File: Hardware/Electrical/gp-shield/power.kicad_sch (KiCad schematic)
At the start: 32 parts, among them J1 XT60/TERM2, J2 XT60/TERM2, Q1 Q_PMOS_GDS, SW1 SW_SPDT, U1 NCP1117-5.0_SOT223, U2 LM4040DBZ-2.5, U4 LM397

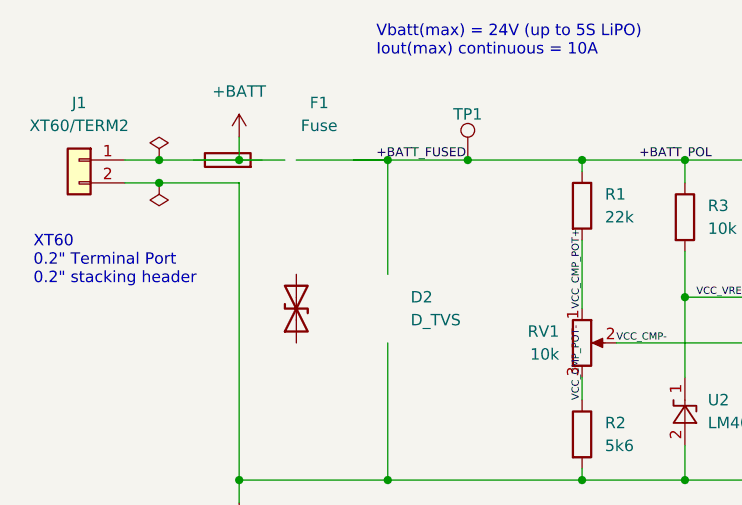
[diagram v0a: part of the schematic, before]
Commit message: Minor annotation fixes from merge
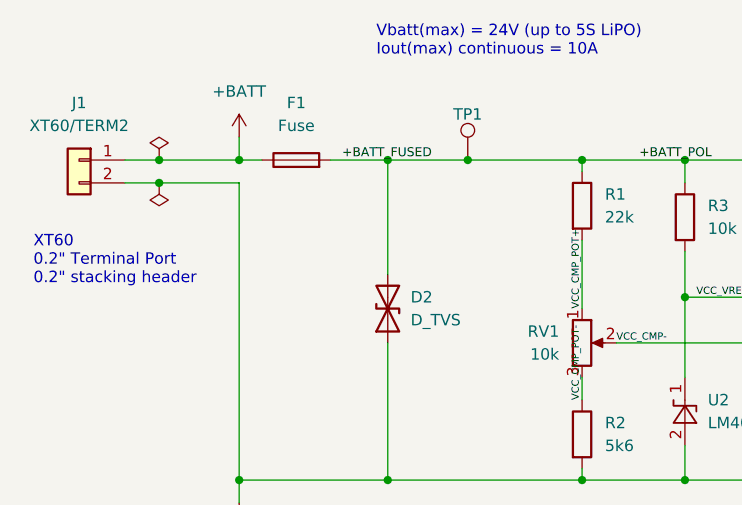
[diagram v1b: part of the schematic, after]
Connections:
- net +BATT: now also F1.1
- net +BATT_FUSED: now also D2.2 (A2), F1.2
- net GND: now also D2.1 (A1)
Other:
- moved on the sheet: D2, F1
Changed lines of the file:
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@@
-    (stroke (width 0) (type default) (color 0 0 0 0))
-  )
-  (wire (pts (xy 58.42 31.75) (xy 62.23 31.75))
     (stroke (width 0) (type default) (color 0 0 0 0))
   )
@@
     (stroke (width 0) (type default) (color 0 0 0 0))
   )
-  (wire (pts (xy 45.72 31.75) (xy 50.8 31.75))
+  (wire (pts (xy 45.72 31.75) (xy 48.26 31.75))
     (stroke (width 0) (type default) (color 0 0 0 0))
   )
@@
     (stroke (width 0) (type default) (color 0 0 0 0))
   )
-  (wire (pts (xy 52.07 31.75) (xy 71.12 31.75))
-    (stroke (width 0) (type default) (color 0 0 0 0))
-  )
   (wire (pts (xy 121.92 39.37) (xy 123.19 39.37))
     (stroke (width 0) (type default) (color 0 0 0 0))
@@
     (stroke (width 0) (type default) (color 0 0 0 0))
   )
+  (wire (pts (xy 55.88 31.75) (xy 62.23 31.75))
+    (stroke (width 0) (type default) (color 0 0 0 0))
+  )
   (wire (pts (xy 87.63 52.07) (xy 106.68 52.07))
     (stroke (width 0) (type default) (color 0 0 0 0))
@@
   )
   (wire (pts (xy 90.17 121.92) (xy 78.74 121.92))
+    (stroke (width 0) (type default) (color 0 0 0 0))
+  )
+  (wire (pts (xy 62.23 31.75) (xy 71.12 31.75))
     (stroke (width 0) (type default) (color 0 0 0 0))
   )
@@
     (effects (font (size 0.8 0.8)) (justify left bottom))
   )
-  (label "+BATT_FUSED" (at 60.96 31.75 0)
+  (label "+BATT_FUSED" (at 57.15 31.75 0)
     (effects (font (size 1 1)) (justify left bottom))
   )
@@
     (pin "1")
   )
-  (symbol (lib_id "Device:D_TVS") (at 52.07 48.26 90) (unit 1)
-    (in_bom yes) (on_board yes) (fields_autoplaced)
-    (property "Reference" "D2" (id 0) (at 64.77 46.9899 90)
+  (symbol (lib_id "Device:D_TVS") (at 62.23 48.26 90) (unit 1)
+    (in_bom yes) (on_board yes)
+    (property "Reference" "D2" (id 0) (at 64.77 46.99 90)
       (effects (font (size 1.27 1.27)) (justify right))
     )
-    (property "Value" "D_TVS" (id 1) (at 64.77 49.5299 90)
+    (property "Value" "D_TVS" (id 1) (at 64.77 49.53 90)
       (effects (font (size 1.27 1.27)) (justify right))
     )
-    (property "Footprint" "Diode_SMD:D_SMA" (id 2) (at 62.23 48.26 0)
-      (effects (font (size 1.27 1.27)) hide)
-    )
-    (property "Datasheet" "~" (id 3) (at 62.23 48.26 0)
+    (property "Footprint" "Diode_SMD:D_SMA" (id 2) (at 72.39 48.26 0)
+      (effects (font (size 1.27 1.27)) hide)
+    )
+    (property "Datasheet" "~" (id 3) (at 72.39 48.26 0)
       (effects (font (size 1.27 1.27)) hide)
     )
@@
     (pin "1")
   )
-  (symbol (lib_id "Device:Fuse") (at 44.45 31.75 90) (unit 1)
-    (in_bom yes) (on_board yes) (fields_autoplaced)
-    (property "Reference" "F1" (id 0) (at 54.61 25.4 90))
-    (property "Value" "Fuse" (id 1) (at 54.61 27.94 90))
-    (property "Footprint" "Fuse:Fuseholder_Littelfuse_445_030_series_5x20mm" (id 2) (at 54.61 33.528 90)
-      (effects (font (size 1.27 1.27)) hide)
-    )
-    (property "Datasheet" "~" (id 3) (at 54.61 31.75 0)
-      (effects (font (size 1.27 1.27)) hide)
-    )
+  (symbol (lib_id "Device:Fuse") (at 52.07 31.75 90) (unit 1)
+    (in_bom yes) (on_board yes)
+    (property "Reference" "F1" (id 0) (at 52.07 25.4 90))
+    (property "Value" "Fuse" (id 1) (at 52.07 27.94 90))
+    (property "Footprint" "Fuse:Fuseholder_Littelfuse_445_030_series_5x20mm" (id 2) (at 62.23 33.528 90)
+      (effects (font (size 1.27 1.27)) hide)
+    )
+    (property "Datasheet" "~" (id 3) (at 62.23 31.75 0)
+      (effects (font (size 1.27 1.27)) hide)
+    )

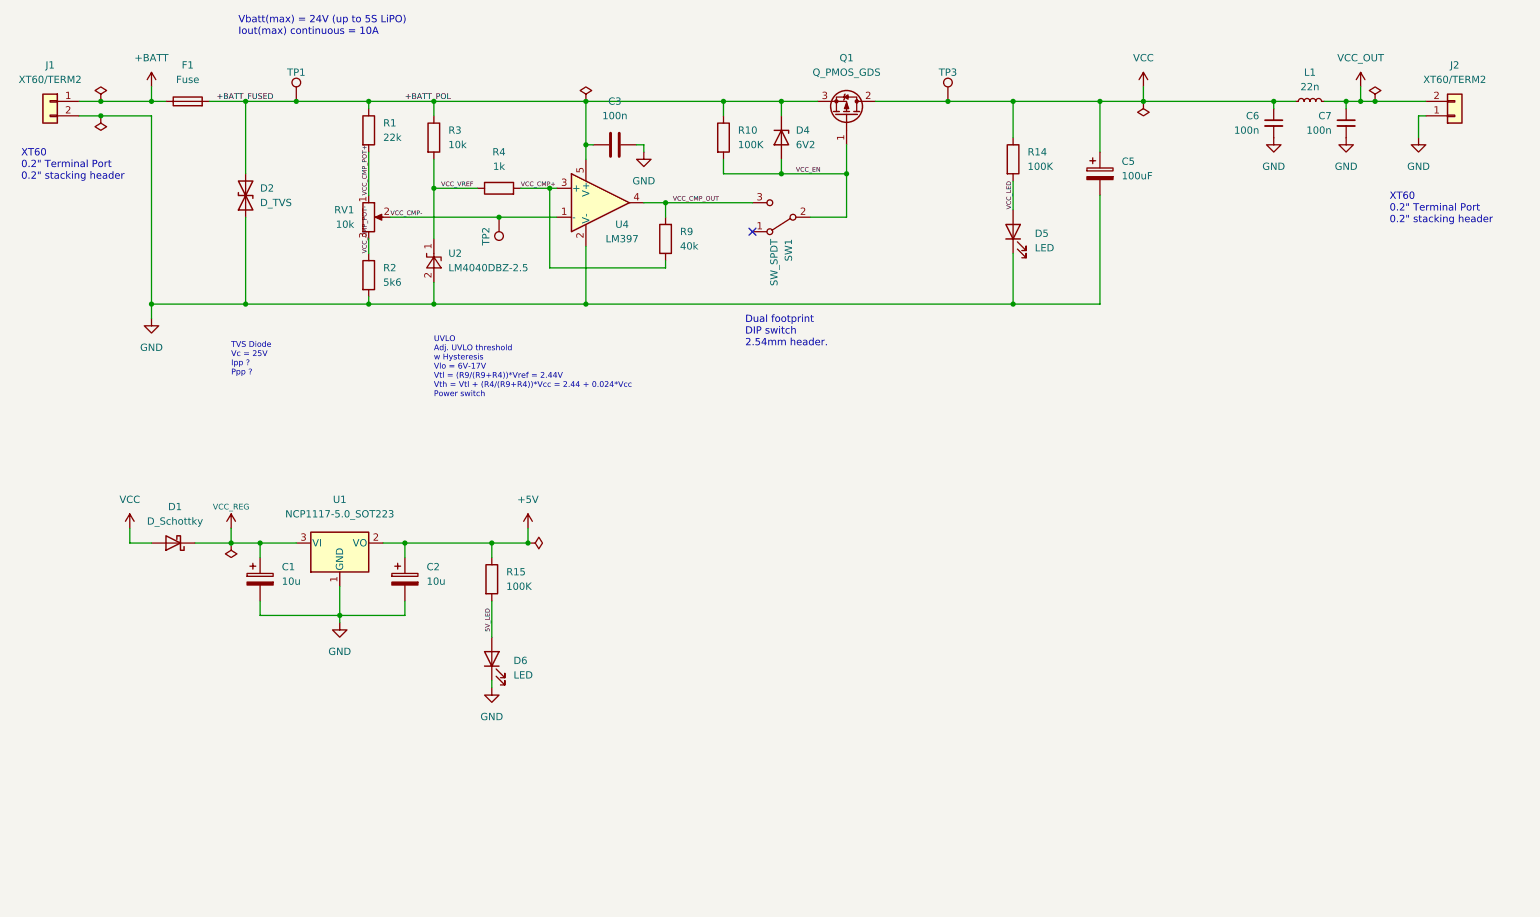
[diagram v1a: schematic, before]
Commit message: Minor changes to annotation and silkscreen
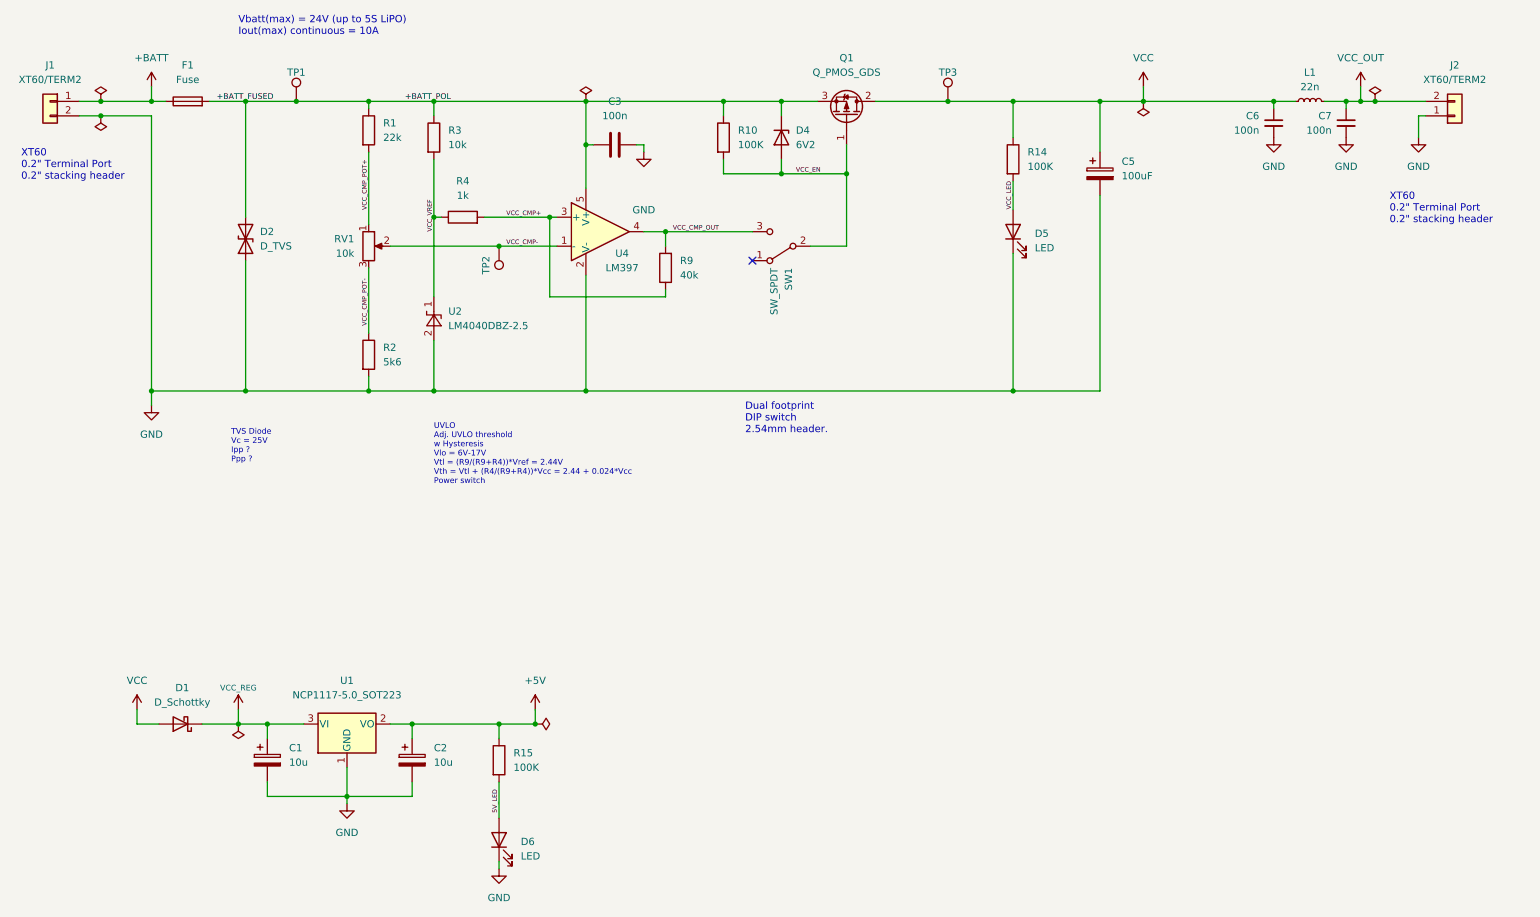
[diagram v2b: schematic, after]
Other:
- moved on the sheet: C1, C2, D1, D2, D6, R15, R2, R4, R9, RV1, SW1, TP2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
